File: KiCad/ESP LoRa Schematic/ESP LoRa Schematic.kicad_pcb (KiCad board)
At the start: 2 copper layers, 141.1 x 141.1 mm, 7 parts, among them U1 ESP32-S3-DEVKITC-1-N8R8, U2 RA-02_LORA

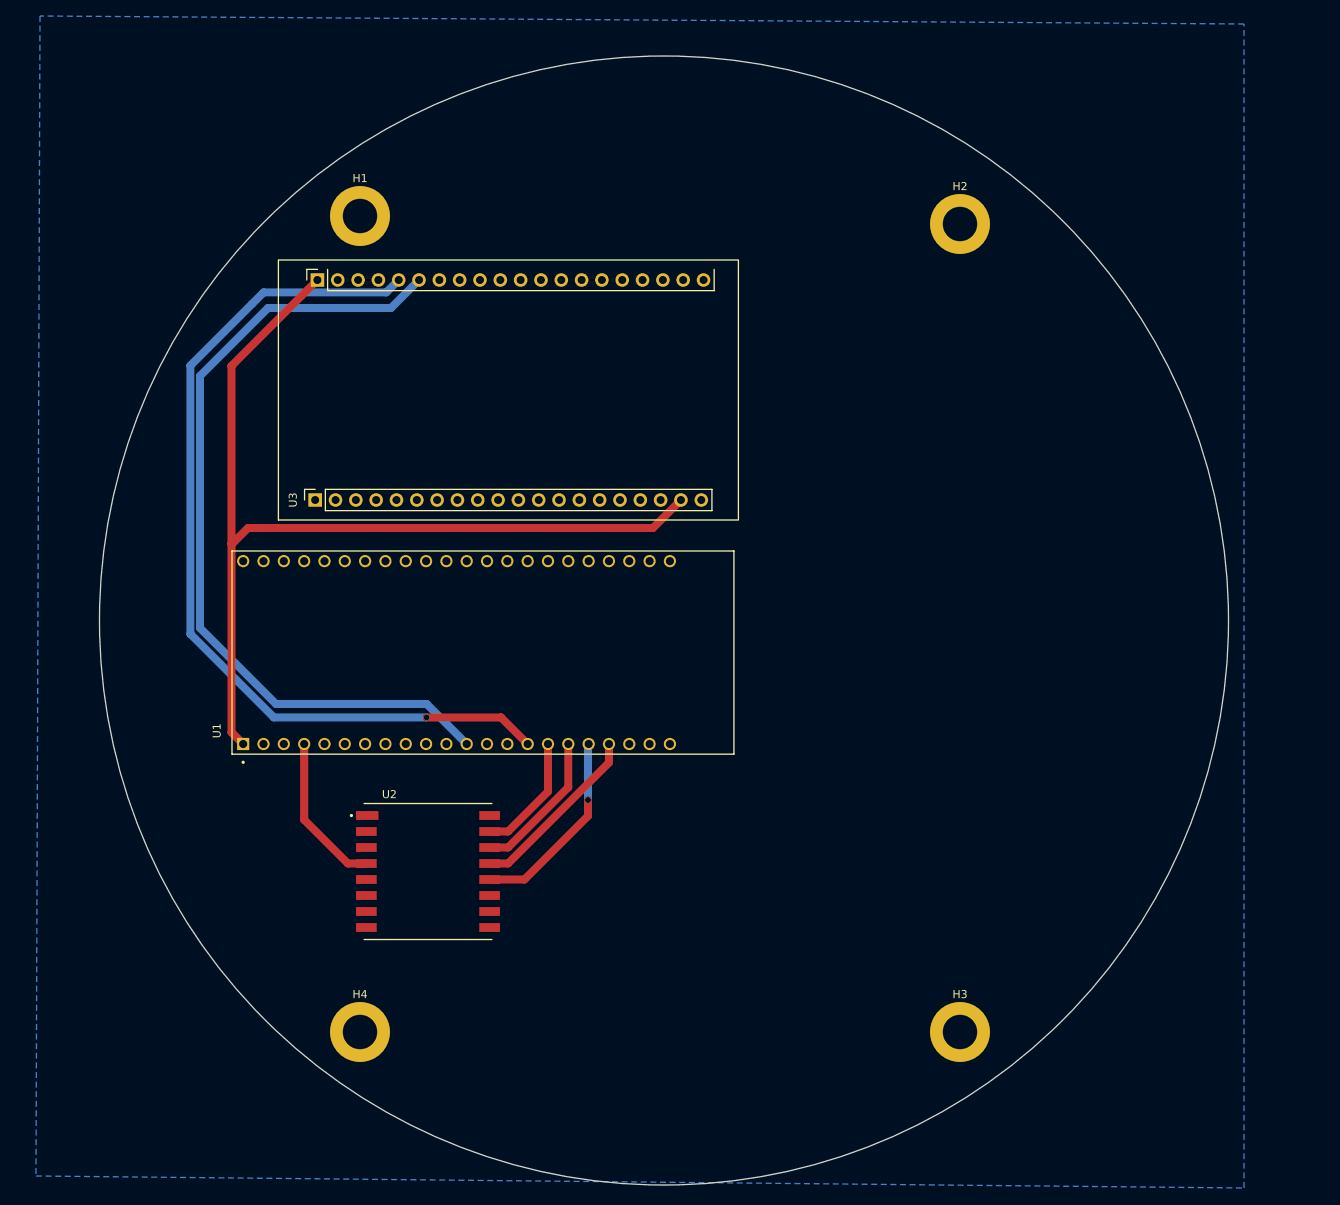
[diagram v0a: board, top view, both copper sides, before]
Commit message: Add Feature
Two side PCB
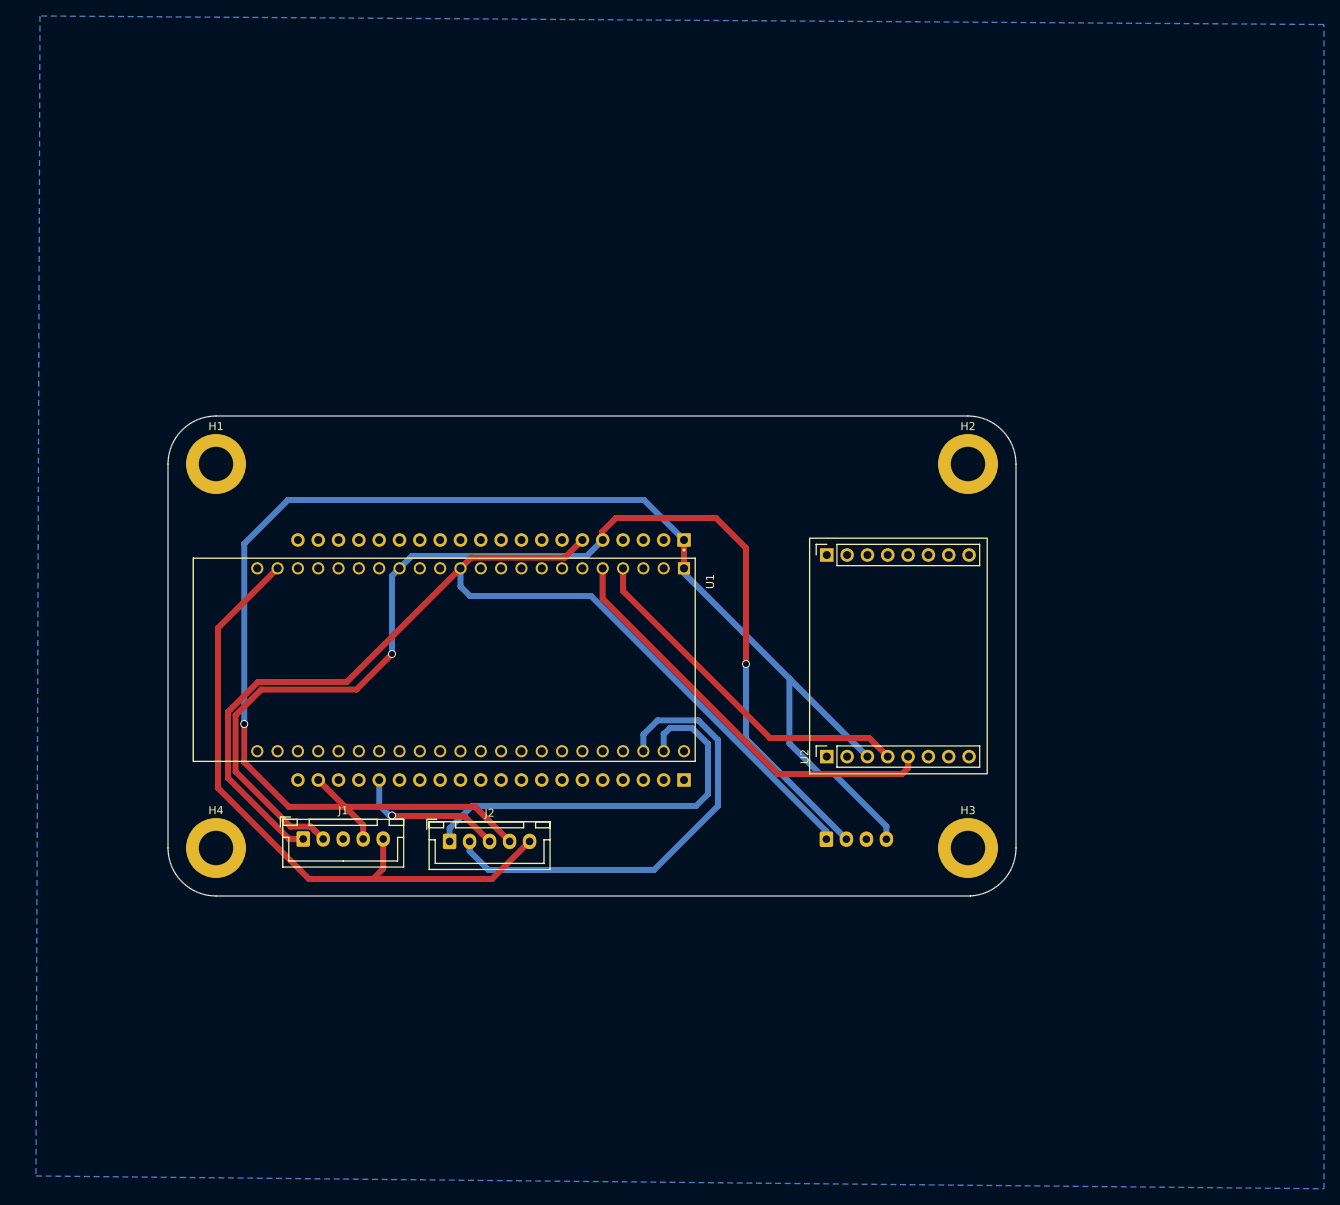
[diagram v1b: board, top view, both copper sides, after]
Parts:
- added J1: Conn_01x05_Socket, Connector_JST:JST_XH_B5B-XH-A_1x05_P2.50mm_Vertical, F.Cu at (86.9, 118.9)
- added J2: Conn_01x05_Socket, Connector_JST:JST_XH_B5B-XH-A_1x05_P2.50mm_Vertical, F.Cu at (105.2, 119.2)
- added OLED1: Conn_01x04_Socket, Connector_JST:JST_XH_B4B-XH-A_1x04_P2.50mm_Vertical, B.Cu at (152.3, 118.9)
- U2: footprint RA-02_LORA:MODULE_RA-02_LORA -> RF:Lora_Dev_Board
- U3: moved to B.Cu
- moved U3 61.0 mm to (136.3, 111.5)
- moved U2 51.9 mm to (152.3, 108.6), turned to 90 degrees
- moved H1 35.8 mm to (76.0, 72.0)
- moved H2 30.0 mm to (170.0, 72.0)
- moved H4 29.2 mm to (76.0, 120.0)
- moved H3 23.0 mm to (170.0, 120.0)
- moved U1 4.92 mm to (104.5, 96.5), turned to -90 degrees
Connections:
- U1 pad J1_21: unconnected-(U1-5V0-PadJ1_21) -> +5V
- U1 pad J1_22: unconnected-(U1-GND3-PadJ1_22) -> GND
- U1 pad J3_2: unconnected-(U1-U0TXD/GPIO43-PadJ3_2) -> GPIO43
- U1 pad J3_21: unconnected-(U1-GND1-PadJ3_21) -> GND
- U1 pad J3_22: unconnected-(U1-GND2-PadJ3_22) -> GND
- U1 pad J3_3: unconnected-(U1-U0RXD/GPIO44-PadJ3_3) -> GPIO44
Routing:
- net +5V: track 0.00 -> 82.1 mm
- net +3.3V: track 121.5 -> 196.7 mm, vias 0 -> 1
- net GPIO44: track 0.00 -> 58.0 mm
- net GPIO5: track 0.00 -> 52.8 mm
- net GPIO43: track 0.00 -> 50.8 mm
- net GPIO9: track 111.9 -> 145.1 mm, vias 1 -> 2
- net GPIO8: track 103.2 -> 135.7 mm
- net GPIO4: track 19.5 -> 44.5 mm
- net GPIO12: track 24.6 -> 0.00 mm, vias 1 -> 0
- net GPIO13: track 22.5 -> 0.00 mm
- net GND: track 0.00 -> 18.8 mm, vias 0 -> 1
- net GPIO11: track 18.4 -> 0.00 mm
- net GPIO10: track 15.3 -> 0.00 mm
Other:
- board size 141.1 x 141.1 mm -> 106 x 60 mm

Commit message: Restructure
added a micropythpon pico project
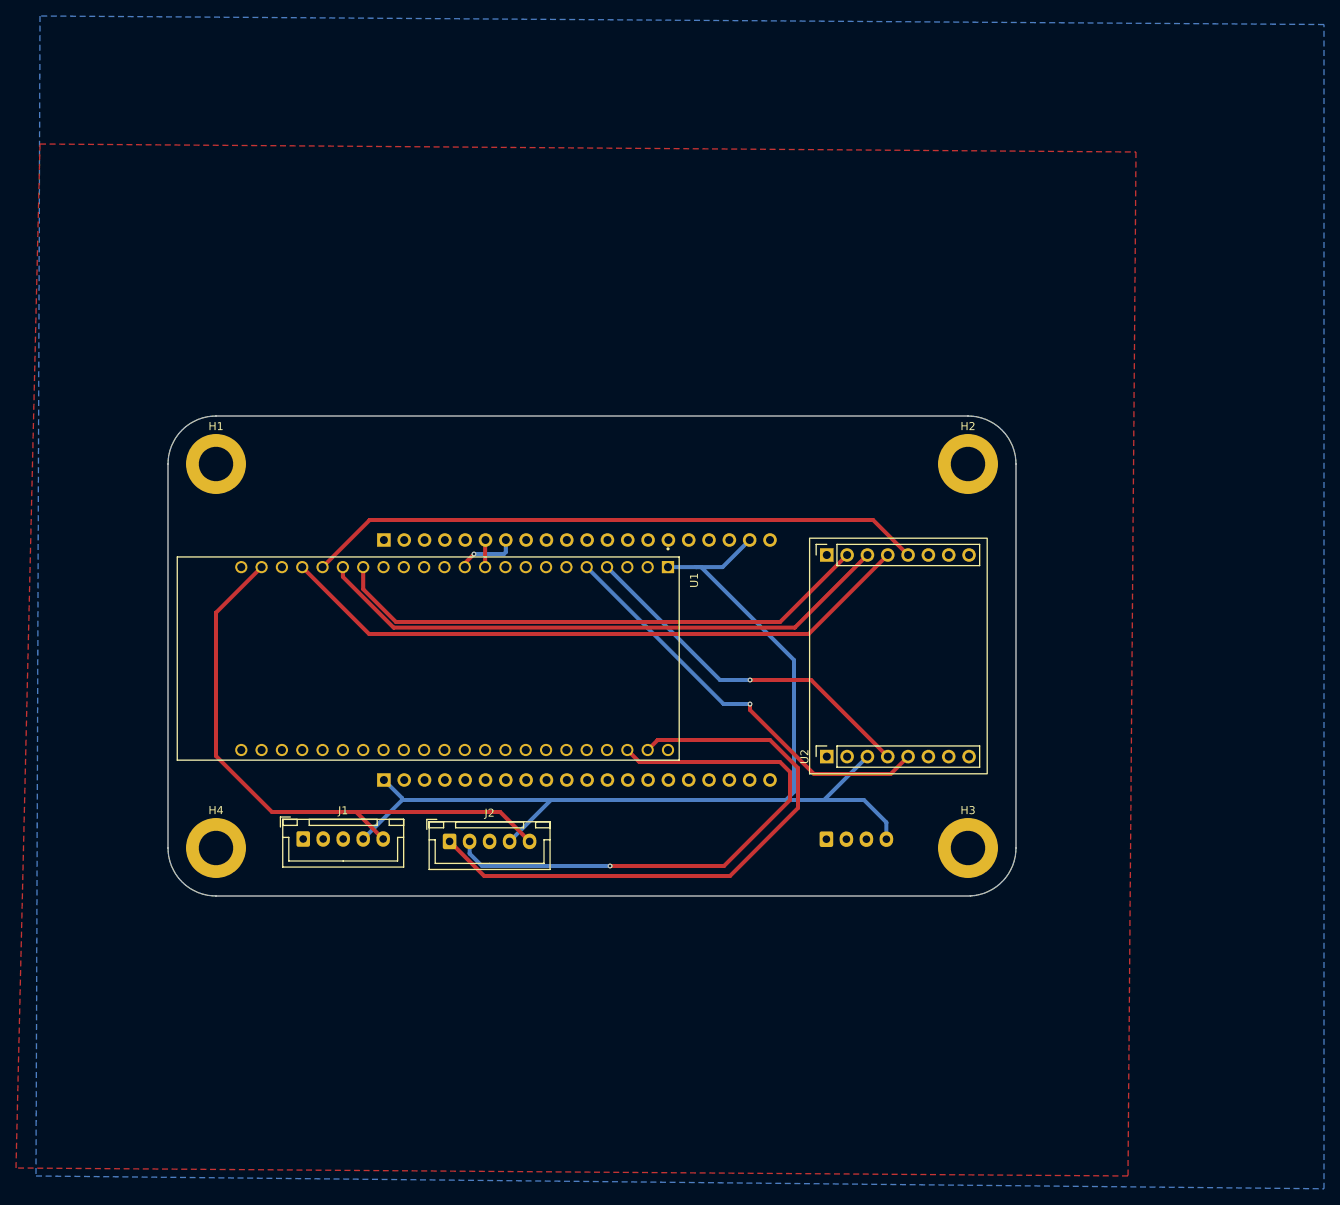
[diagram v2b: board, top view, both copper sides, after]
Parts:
- moved U3 50.9 mm to (95.2, 81.5), turned to -90 degrees
- moved U1 2.01 mm to (102.5, 96.3)
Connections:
- U1 pad J1_10: unconnected-(U1-GPIO17-PadJ1_10) -> GPIO17
- U1 pad J1_11: unconnected-(U1-GPIO18-PadJ1_11) -> GPIO18
- U1 pad J1_12: GPIO8 -> unconnected-(U1-GPIO8-PadJ1_12)
- U1 pad J1_15: GPIO9 -> unconnected-(U1-GPIO9-PadJ1_15)
- U3 pad 25: GPIO9 -> unconnected-(U3-I2C1_SCL-Pad25)
- U3 pad 26: GPIO8 -> unconnected-(U3-I2C1_SDA-Pad26)
- U3 pad 6: unconnected-(U3-TX1-Pad6) -> GPIO17
- U3 pad 7: unconnected-(U3-RX1-Pad7) -> GPIO18
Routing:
- net GPIO9: track 145.1 -> 0.00 mm, vias 2 -> 0
- net GPIO8: track 135.7 -> 0.00 mm
- net GPIO13: track 0.00 -> 80.7 mm
- net GPIO12: track 0.00 -> 77.4 mm
- net GPIO11: track 0.00 -> 73.2 mm
- net GPIO10: track 0.00 -> 68.4 mm
- net +3.3V: track 196.7 -> 136.6 mm, vias 1 -> 0
- net GPIO43: track 50.8 -> 74.6 mm
- net GND: track 18.8 -> 0.00 mm, vias 1 -> 0
- net GPIO44: track 58.0 -> 70.6 mm, vias 0 -> 1
- net GPIO18: track 0.00 -> 7.71 mm, vias 0 -> 1
- net +5V: track 82.1 -> 74.9 mm
- net GPIO17: track 0.00 -> 3.41 mm
- net GPIO5: track 52.8 -> 52.2 mm, vias 0 -> 1
- net GPIO4: track 44.5 -> 44.9 mm, vias 0 -> 1
- added copper zone on F.Cu, net GND

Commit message: add feature
add second UART line for configureing UART
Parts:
- added kibuzzard-69B7B2E3: G***, kibuzzard-69B7B2E3, F.Cu at (159.0, 72.0)
- added kibuzzard-69B7B320: G***, kibuzzard-69B7B320, F.Cu at (152.0, 80.0)
- J2: value Conn_01x05_Socket -> Conn_01x02_Socket; footprint Connector_JST:JST_XH_B5B-XH-A_1x05_P2.50mm_Vertical -> Connector_JST:JST_XH_B2B-XH-A_1x02_P2.50mm_Vertical
- moved J2 51.1 mm to (87.5, 71.2)
- moved OLED1 7.45 mm to (159.8, 118.9), turned to 180 degrees
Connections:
- J2 pad 1: GPIO43 -> +5V
- J2 pad 2: GPIO44 -> GND
- OLED1 pad 1: GPIO8 -> GND
- OLED1 pad 2: GPIO9 -> +3.3V
- OLED1 pad 3: GND -> GPIO9
- OLED1 pad 4: +3.3V -> GPIO8
- U1 pad J1_12: unconnected-(U1-GPIO8-PadJ1_12) -> GPIO8
- U1 pad J1_15: unconnected-(U1-GPIO9-PadJ1_15) -> GPIO9
- U1 pad J1_6: unconnected-(U1-GPIO6-PadJ1_6) -> GPIO6
- U1 pad J1_7: unconnected-(U1-GPIO7-PadJ1_7) -> GPIO7
- U1 pad J1_8: unconnected-(U1-GPIO15-PadJ1_8) -> GPIO15
- U1 pad J3_2: GPIO43 -> unconnected-(U1-U0TXD/GPIO43-PadJ3_2)
- U1 pad J3_3: GPIO44 -> unconnected-(U1-U0RXD/GPIO44-PadJ3_3)
- U3 pad 24: unconnected-(U3-NRST-Pad24) -> GPIO15
- U3 pad 30: unconnected-(U3-PA2-Pad30) -> GPIO17
- U3 pad 31: unconnected-(U3-PA3-Pad31) -> GPIO18
- U3 pad 6: GPIO17 -> GPIO6
- U3 pad 7: GPIO18 -> GPIO7
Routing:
- net GPIO9: track 0.00 -> 135.2 mm
- net GPIO8: track 0.00 -> 134.0 mm
- net GPIO17: track 3.41 -> 97.8 mm
- net GPIO18: track 7.71 -> 101.4 mm, vias 1 -> 0
- net GPIO43: track 74.6 -> 0.00 mm
- net GPIO15: track 0.00 -> 71.7 mm
- net GPIO44: track 70.6 -> 0.00 mm, vias 1 -> 0
- net +3.3V: track 136.6 -> 176.0 mm, vias 0 -> 1
- net GPIO6: track 0.00 -> 11.5 mm
- net GPIO7: track 0.00 -> 6.43 mm
- net GPIO12: track 77.4 -> 82.0 mm
- net GPIO13: track 80.7 -> 77.4 mm
- net +5V: track 74.9 -> 72.3 mm
- net GPIO4: track 44.9 -> 46.6 mm, vias 1 -> 0
- net GPIO11: track 73.2 -> 73.9 mm
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
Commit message: New Egg Folder
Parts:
- moved U3 49.0 mm to (134.3, 111.0), turned to 90 degrees
- moved OLED1 25.7 mm to (134.2, 120.7), turned to 0 degrees
- moved U2 25.6 mm to (156.9, 83.4), turned to -90 degrees
- moved H2 16.0 mm to (154.0, 72.0)
- moved H3 16.0 mm to (154.0, 120.0)
- moved kibuzzard-69B7B2E3 15.6 mm to (143.4, 71.5)
- moved kibuzzard-69B7B320 1.80 mm to (150.2, 80.0)
- moved U1 0.15 mm to (102.5, 96.5)
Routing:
- net +3.3V: track 176.0 -> 0.00 mm, vias 1 -> 0
- net GPIO9: track 135.2 -> 0.00 mm
- net GPIO8: track 134.0 -> 0.00 mm
- net GPIO18: track 101.4 -> 0.00 mm
- net GPIO17: track 97.8 -> 0.00 mm
- net GPIO12: track 82.0 -> 0.00 mm
- net GPIO13: track 77.4 -> 0.00 mm
- net GPIO11: track 73.9 -> 0.00 mm
- net +5V: track 72.3 -> 0.28 mm
- net GPIO15: track 71.7 -> 0.00 mm
- net GPIO10: track 69.2 -> 0.00 mm
- net GPIO5: track 51.8 -> 0.00 mm
- net GPIO4: track 46.6 -> 0.00 mm
- net GPIO6: track 11.5 -> 0.00 mm
- net GPIO7: track 6.43 -> 0.00 mm
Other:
- board size 106 x 60 mm -> 90 x 60 mm
